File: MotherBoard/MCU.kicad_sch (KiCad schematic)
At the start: 0 parts

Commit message: Added IO Connector and uC
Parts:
- added U1: STM32F205RBTx, Package_QFP:LQFP-64_10x10mm_P0.5mm, symbol MCU_ST_STM32F2:STM32F205RBTx
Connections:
- new net: U1.18 (VSS), U1.63 (VSS)
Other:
- company: (none) -> FSAE LSU
- title: (none) -> STM32 Layout
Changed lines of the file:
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@@
 	(generator_version "8.0")
 	(paper "A4")
+	(title_block
+		(title "STM32 Layout")
+		(date "2024-10-15")
+		(rev "A")
+		(company "FSAE LSU")
+	)
+	(symbol
+		(lib_id "MCU_ST_STM32F2:STM32F205RBTx")
+		(at 143.51 92.71 0)
+		(unit 1)
+		(exclude_from_sim no)
+		(in_bom yes)
+		(on_board yes)
+		(dnp no)
+		(fields_autoplaced yes)
+		(property "Reference" "U1"
+			(at 148.2441 138.43 0)
+			(effects
+				(font
+					(size 1.27 1.27)
+				)
+				(justify left)
+			)
+		)
+		(property "Value" "STM32F205RBTx"
+			(at 148.2441 140.97 0)
+			(effects
+				(font
+					(size 1.27 1.27)
+				)
+				(justify left)
+			)
+		)
+		(property "Footprint" "Package_QFP:LQFP-64_10x10mm_P0.5mm"
+			(at 128.27 135.89 0)
+			(effects
+				(font
+					(size 1.27 1.27)
+				)
+				(justify right)
+				(hide yes)
+			)
+		)
+		(property "Datasheet" "https://www.st.com/resource/en/datasheet/stm32f205rb.pdf"
+			(at 143.51 92.71 0)
+			(effects
+				(font
+					(size 1.27 1.27)
+				)
+				(hide yes)
+			)
+		)
+		(property "Description" "STMicroelectronics Arm Cortex-M3 MCU, 128KB flash, 64KB RAM, 120 MHz, 1.8-3.6V, 51 GPIO, LQFP64"
+			(at 143.51 92.71 0)
+			(effects
+				(font
+					(size 1.27 1.27)
+				)
+				(hide yes)
+			)
+		)
+		(pin "46"
+		)
+		(pin "54"
+		)
+		(pin "58"
+		)
+		(pin "23"
+		)
+		(pin "16"
+		)
+		(pin "37"
+		)
+		(pin "44"
+		)
+		(pin "21"
+		)
+		(pin "38"
+		)
+		(pin "10"
+		)
+		(pin "45"
+		)
+		(pin "51"
+		)
+		(pin "52"
+		)
+		(pin "14"
+		)
+		(pin "36"
+		)
+		(pin "59"
+		)
+		(pin "18"
+		)
+		(pin "61"
+		)
+		(pin "62"
+		)
+		(pin "63"
+		)
+		(pin "15"
+		)
+		(pin "42"
+		)
+		(pin "43"
+		)
+		(pin "35"
+		)
+		(pin "29"
+		)
+		(pin "41"
+		)
+		(pin "53"
+		)
+		(pin "27"
+		)
+		(pin "33"
+		)
+		(pin "6"
+		)
+		(pin "2"
+		)
+		(pin "64"
+		)
+		(pin "26"
+		)
+		(pin "56"
+		)
+		(pin "47"
+		)
+		(pin "7"
+		)
+		(pin "4"
+		)
+		(pin "48"
+		)
+		(pin "34"
+		)
+		(pin "32"
+		)
+		(pin "40"
+		)
+		(pin "5"
+		)
+		(pin "60"
+		)
+		(pin "13"
+		)
+		(pin "22"
+		)
+		(pin "1"
+		)
+		(pin "20"
+		)
+		(pin "24"
+		)
+		(pin "39"
+		)
+		(pin "49"
+		)
+		(pin "31"
+		)
+		(pin "19"
+		)
+		(pin "55"
+		)
+		(pin "57"
+		)
+		(pin "8"
+		)
+		(pin "17"
+		)
+		(pin "28"
+		)
+		(pin "11"
+		)
+		(pin "25"
+		)
+		(pin "30"
+		)
+		(pin "3"
+		)
+		(pin "50"
+		)
+		(pin "12"
+		)
+		(pin "9"
+		)
+		(instances
+			(project ""
+				(path "/335e81e9-b957-4266-8116-dde74329bfca/592735c9-cbc0-4c76-b37a-83bb0c07029e"
+					(reference "U1")
+					(unit 1)
+				)
+			)
+		)
+	)
 )

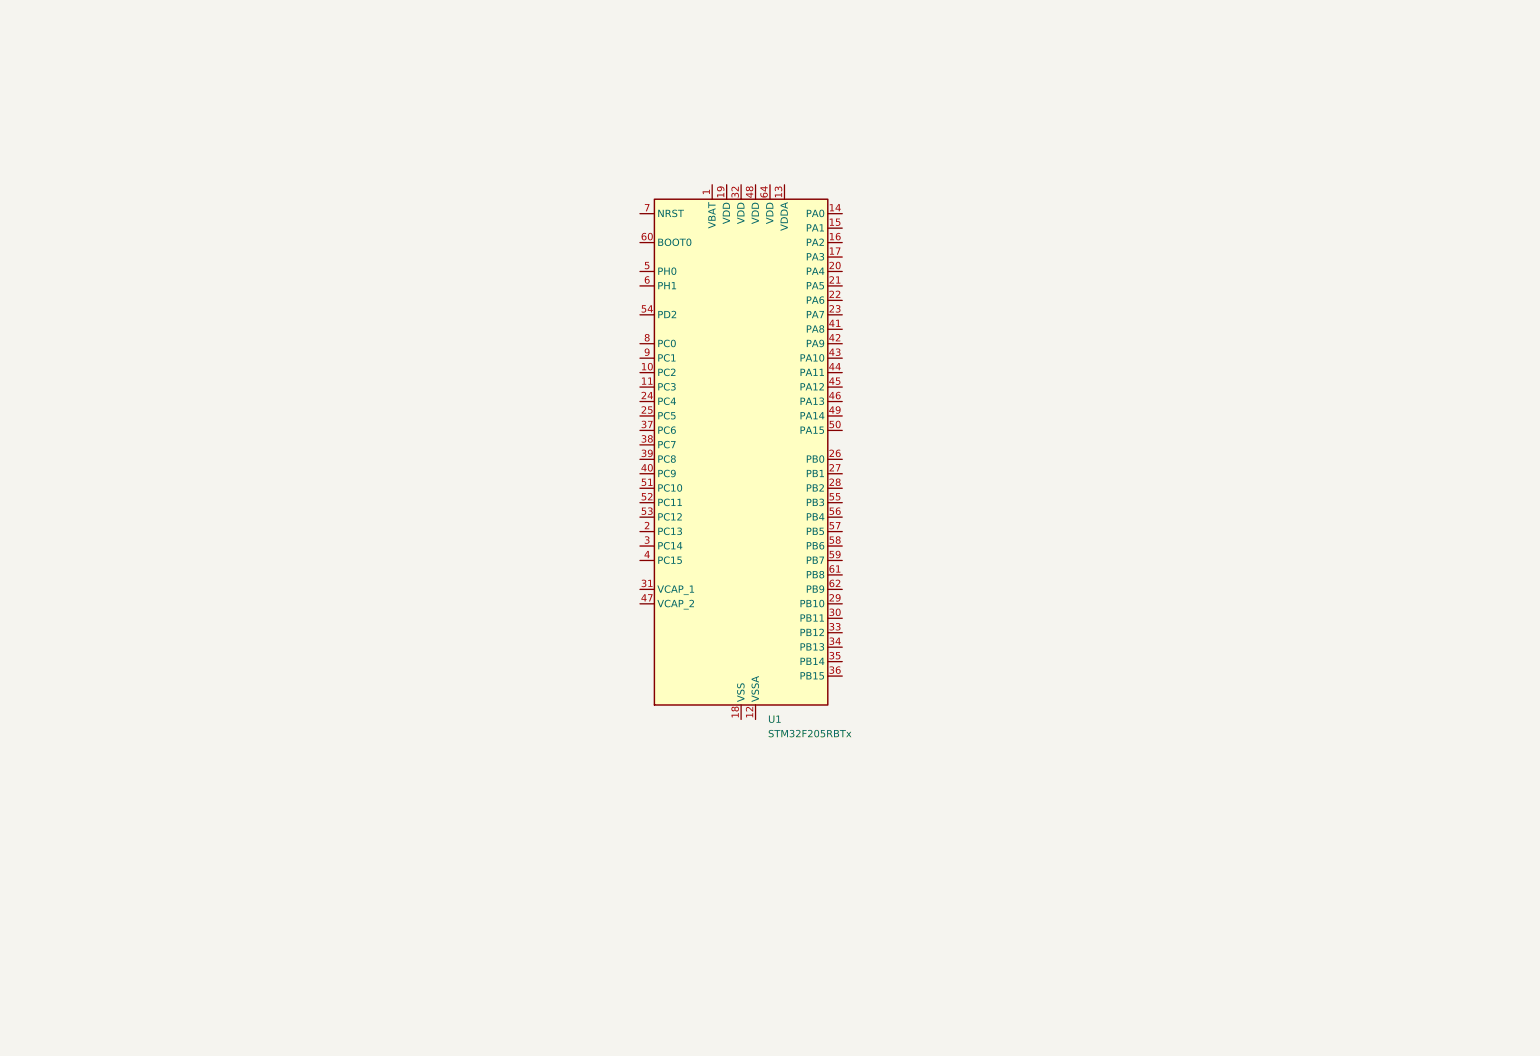
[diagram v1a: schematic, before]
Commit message: Complete bootstrap schematic for MCU
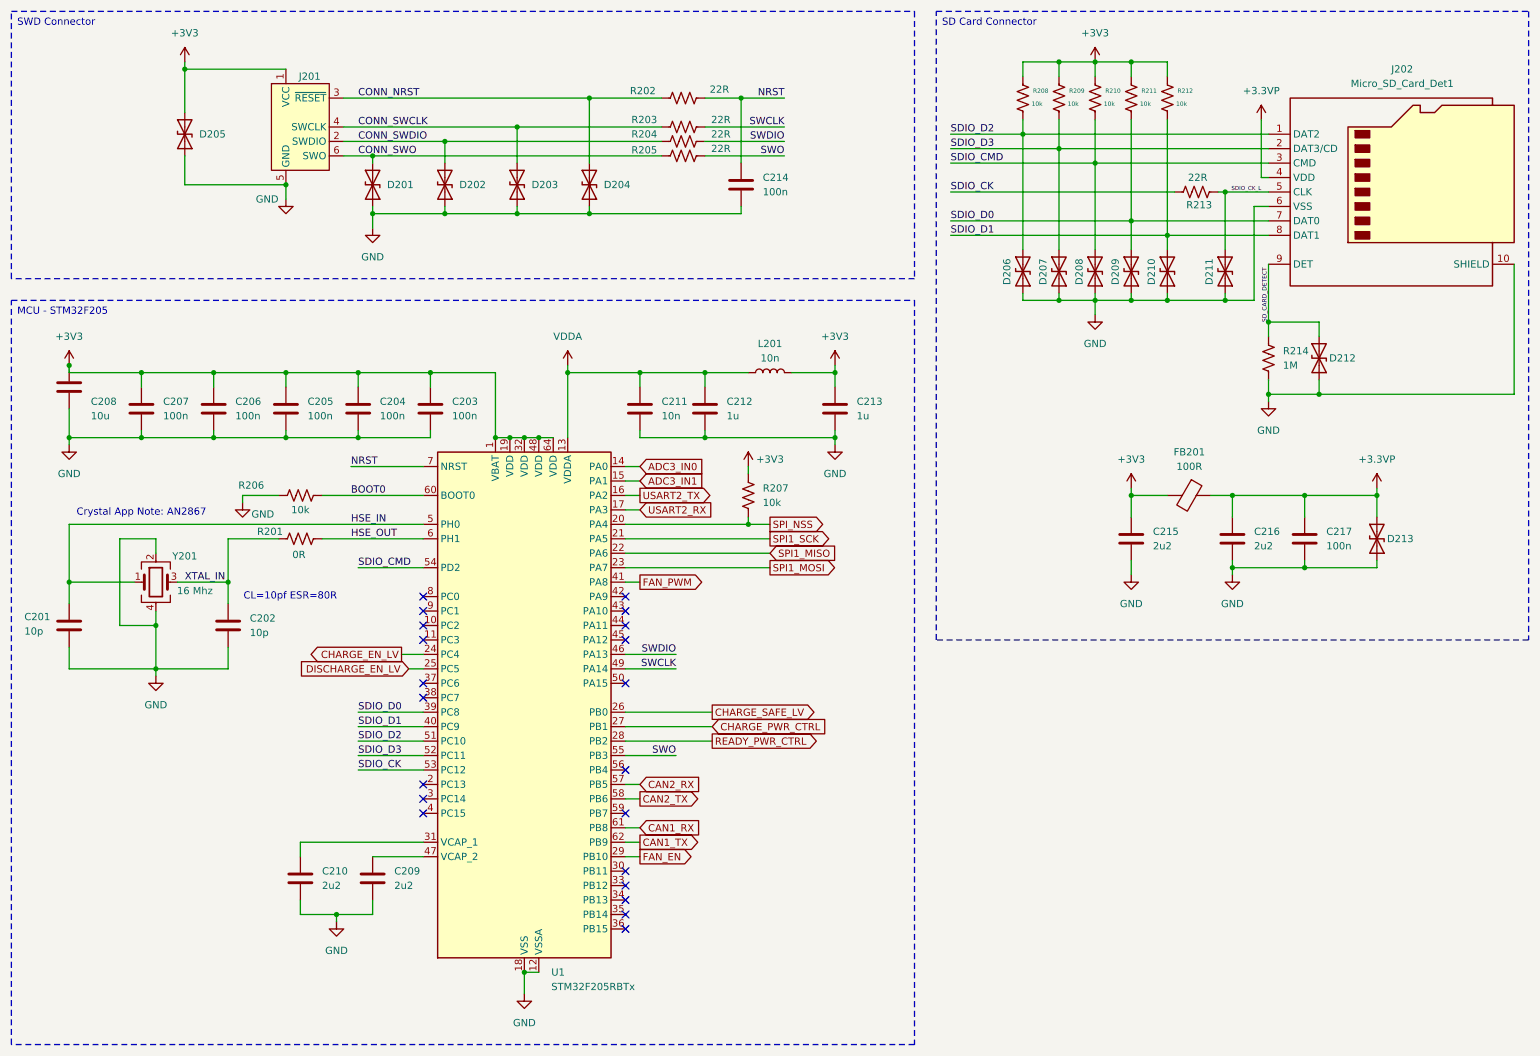
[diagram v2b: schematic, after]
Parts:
- added C201, C202: 10p, symbol Device:C
- added C203, C204, C205, C206, C207, C214, C217: 100n, symbol Device:C
- added C208: 10u, symbol Device:C
- added C209, C210, C215, C216: 2u2, symbol Device:C
- added C211: 10n, symbol Device:C
- added C212, C213: 1u, symbol Device:C
- added D201, D202, D203, D204, D205, D206, D207, D208, D209, D210, D211, D212, D213: 1N630xCA, Diode_THT:D_DO-201AE_P15.24mm_Horizontal, symbol Diode:1N630xCA
- added FB201: 100R, symbol Device:FerriteBead
- added J201: Conn_ARM_SWD_TagConnect_TC2030, Connector:Tag-Connect_TC2030-IDC-FP_2x03_P1.27mm_Vertical, symbol Connector:Conn_ARM_SWD_TagConnect_TC2030
- added J202: Micro_SD_Card_Det1, symbol Connector:Micro_SD_Card_Det1
- added L201: 10n, symbol Device:L
- added R201: 0R, symbol Device:R_US
- added R202, R203, R204, R205, R213: 22R, symbol Device:R_US
- added R206, R207, R208, R209, R210, R211, R212: 10k, symbol Device:R_US
- added R214: 1M, symbol Device:R_US
- added Y201: 16 Mhz, Crystal:Crystal_SMD_3225-4Pin_3.2x2.5mm, symbol Device:Crystal_GND24
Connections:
- net +3V3: now reaches U1.1 (VBAT)
- net +3V3: now also U1.19 (VDD), U1.32 (VDD), U1.48 (VDD), U1.64 (VDD), C203.1, C204.1, C205.1, C206.1, C207.1, C208.1, C213.1, C215.1, D205.2 (A2), FB201.2, J201.1 (VCC), L201.2, R207.1, R208.1, R209.1, R210.1, R211.1, R212.1
- net GND: now reaches U1.12 (VSSA)
- net GND: now also U1.18 (VSS), U1.63 (VSS), C201.2, C202.2, C203.2, C204.2, C205.2, C206.2, C207.2, C208.2, C209.2, C210.2, C211.2, C212.2, C213.2, C214.2, C215.2, C216.2, C217.2, D201.1 (A1), D202.1 (A1), D203.1 (A1), D204.1 (A1), D205.1 (A1), D206.1 (A1), D207.1 (A1), D208.1 (A1), D209.1 (A1), D210.1 (A1), D211.1 (A1), D212.1 (A1), D213.1 (A1), J201.5 (GND), J202.10 (SHIELD), J202.6 (VSS), R206.2, R214.2, Y201.2, Y201.4
- net VDDA: now reaches U1.13 (VDDA)
- net VDDA: now also C211.1, C212.1, L201.1
- net ADC3_IN0: now reaches U1.14 (PA0)
- net ADC3_IN1: now reaches U1.15 (PA1)
- net USART2_TX: now reaches U1.16 (PA2)
- net USART2_RX: now reaches U1.17 (PA3)
- net SPI_NSS: now reaches U1.20 (PA4)
- net SPI_NSS: now also R207.2
- net SPI1_SCK: now reaches U1.21 (PA5)
- net SPI1_MISO: now reaches U1.22 (PA6)
- net SPI1_MOSI: now reaches U1.23 (PA7)
- net CHARGE_EN_LV: now reaches U1.24 (PC4)
- net DISCHARGE_EN_LV: now reaches U1.25 (PC5)
- net CHARGE_SAFE_LV: now reaches U1.26 (PB0)
- net CHARGE_PWR_CTRL: now reaches U1.27 (PB1)
- net READY_PWR_CTRL: now reaches U1.28 (PB2)
- net FAN_EN: now reaches U1.29 (PB10)
- net at U1.31 (VCAP_1): now also C210.1
- net SDIO_D0: now reaches U1.39 (PC8)
- net SDIO_D0: now also D209.2 (A2), J202.7 (DAT0), R211.2
- net SDIO_D1: now reaches U1.40 (PC9)
- net SDIO_D1: now also D210.2 (A2), J202.8 (DAT1), R212.2
- net FAN_PWM: now reaches U1.41 (PA8)
- net SWDIO: now reaches U1.46 (PA13)
- net SWDIO: now also R204.2
- net at U1.47 (VCAP_2): now also C209.1
- net SWCLK: now reaches U1.49 (PA14)
- net SWCLK: now also R203.2
- net HSE_IN: now reaches U1.5 (PH0)
- net HSE_IN: now also C201.1, Y201.1
- net SDIO_D2: now reaches U1.51 (PC10)
- net SDIO_D2: now also D206.2 (A2), J202.1 (DAT2), R208.2
- net SDIO_D3: now reaches U1.52 (PC11)
- net SDIO_D3: now also D207.2 (A2), J202.2 (DAT3/CD), R209.2
- net SDIO_CK: now reaches U1.53 (PC12)
- net SDIO_CK: now also R213.1
- net SDIO_CMD: now reaches U1.54 (PD2)
- net SDIO_CMD: now also D208.2 (A2), J202.3 (CMD), R210.2
- net SWO: now reaches U1.55 (PB3)
- net SWO: now also R205.2
- net CAN2_RX: now reaches U1.57 (PB5)
- net CAN2_TX: now reaches U1.58 (PB6)
- net HSE_OUT: now reaches U1.6 (PH1)
- net HSE_OUT: now also R201.2
- net BOOT0: now reaches U1.60 (BOOT0)
- net BOOT0: now also R206.1
- net CAN1_RX: now reaches U1.61 (PB8)
- net CAN1_TX: now reaches U1.62 (PB9)
- net NRST: now reaches U1.7 (NRST)
- net NRST: now also C214.1, R202.2
- new net +3.3VP: C216.1, C217.1, D213.2 (A2), FB201.1, J202.4 (VDD)
- new net CONN_NRST: D204.2 (A2), J201.3 (~{RESET}), R202.1
- new net CONN_SWCLK: D203.2 (A2), J201.4 (SWCLK), R203.1
- new net CONN_SWDIO: D202.2 (A2), J201.2 (SWDIO), R204.1
- new net CONN_SWO: D201.2 (A2), J201.6 (SWO), R205.1
- new net SDIO_CK_L: D211.2 (A2), J202.5 (CLK), R213.2
- new net SD_CARD_DETECT: D212.2 (A2), J202.9 (DET), R214.1
- new net XTAL_IN: C202.1, R201.1, Y201.3
- no-connect marks 0 -> 21
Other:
- note added: "CL=10pf ESR=80R"
- note added: "Crystal App Note: AN2867"
- moved on the sheet: U1

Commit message: PSU Complete
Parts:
- removed D207, D208, D209, D210, D211: 1N630xCA, Diode_THT:D_DO-201AE_P15.24mm_Horizontal, symbol Diode:1N630xCA
- added D207, D208, D209, D210, D211: D_TVS, Diode_SMD:D_SOD-323, symbol Device:D_TVS
- D201: renamed from D205; value 1N630xCA -> D_TVS; footprint Diode_THT:D_DO-201AE_P15.24mm_Horizontal -> Diode_SMD:D_SOD-323; symbol Diode:1N630xCA -> Device:D_TVS
- D202: renamed from D201; value 1N630xCA -> D_TVS; footprint Diode_THT:D_DO-201AE_P15.24mm_Horizontal -> Diode_SMD:D_SOD-323; symbol Diode:1N630xCA -> Device:D_TVS
- D203: renamed from D202; value 1N630xCA -> D_TVS; footprint Diode_THT:D_DO-201AE_P15.24mm_Horizontal -> Diode_SMD:D_SOD-323; symbol Diode:1N630xCA -> Device:D_TVS
- D204: renamed from D203; value 1N630xCA -> D_TVS; footprint Diode_THT:D_DO-201AE_P15.24mm_Horizontal -> Diode_SMD:D_SOD-323; symbol Diode:1N630xCA -> Device:D_TVS
- D205: renamed from D204; value 1N630xCA -> D_TVS; footprint Diode_THT:D_DO-201AE_P15.24mm_Horizontal -> Diode_SMD:D_SOD-323; symbol Diode:1N630xCA -> Device:D_TVS
- D206, D212, D213: value 1N630xCA -> D_TVS; footprint Diode_THT:D_DO-201AE_P15.24mm_Horizontal -> Diode_SMD:D_SOD-323; symbol Diode:1N630xCA -> Device:D_TVS
- R201: renamed from R206; footprint (none) -> Resistor_SMD:R_0402_1005Metric
- R202: renamed from R201; footprint (none) -> Resistor_SMD:R_0402_1005Metric
- R203: renamed from R202; footprint (none) -> Resistor_SMD:R_0402_1005Metric
- R204: renamed from R203; footprint (none) -> Resistor_SMD:R_0402_1005Metric
- R205: renamed from R204; footprint (none) -> Resistor_SMD:R_0402_1005Metric
- R206: renamed from R205; footprint (none) -> Resistor_SMD:R_0402_1005Metric
- R207, R208, R209, R210, R211, R212, R213, R214: footprint (none) -> Resistor_SMD:R_0402_1005Metric
- renumbered C208 to C201, C201 to C202, C207 to C203, C206 to C204, C202 to C205, C205 to C206, C210 to C207, C204 to C208, C203 to C210, C214 to C213, C213 to C214, U1 to U201
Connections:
- net GND: now also D207.1 (A1), D208.1 (A1), D209.1 (A1), D210.1 (A1), D211.1 (A1)
- net SDIO_CK_L: now also D211.2 (A2)
- net SDIO_CMD: now also D208.2 (A2)
- net SDIO_D0: now also D209.2 (A2)
- net SDIO_D1: now also D210.2 (A2)
- net SDIO_D3: now also D207.2 (A2)
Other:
- note added: "100mA Max"
- note added: "120mA Max ~40mA Typ"
- note added: ">2 Ohm ESR"

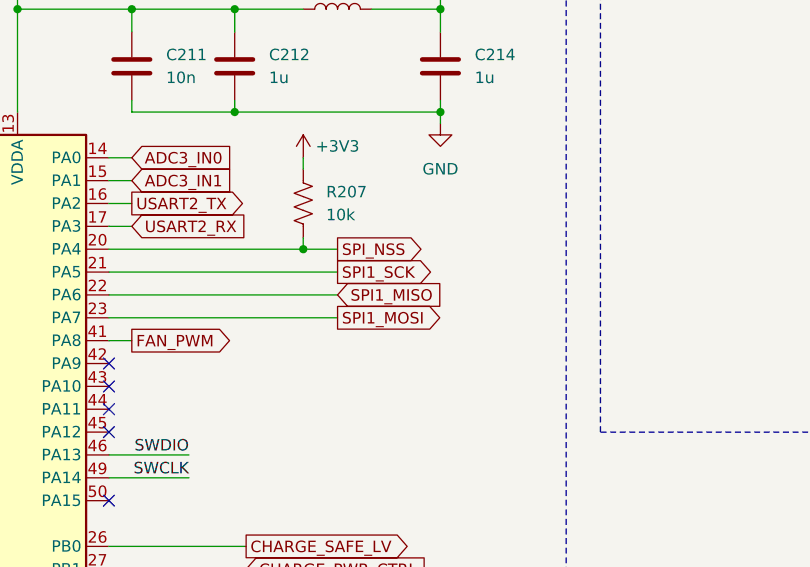
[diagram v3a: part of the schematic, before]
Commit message: Added BQ7900 rough draft and TCAN
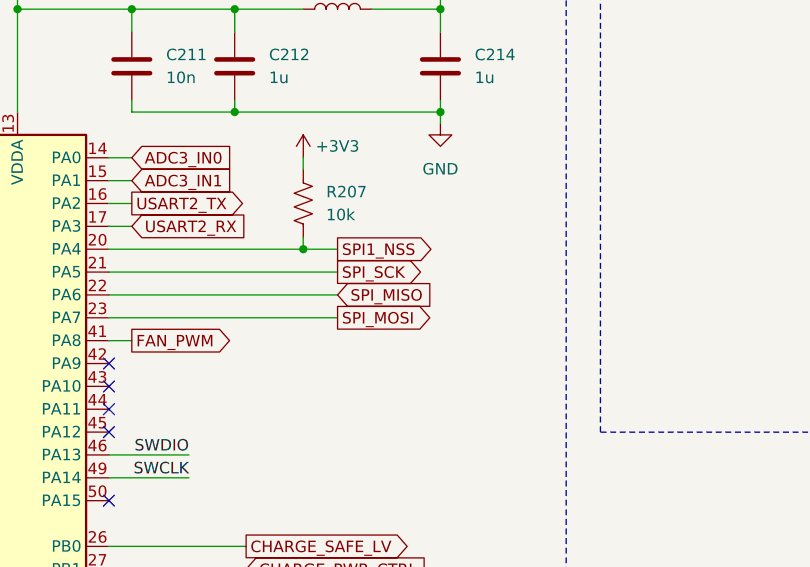
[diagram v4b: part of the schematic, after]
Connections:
- net SPI1_MISO renamed SPI_MISO
- net SPI1_MOSI renamed SPI_MOSI
- net SPI1_SCK renamed SPI_SCK
- net SPI_NSS renamed SPI1_NSS
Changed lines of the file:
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@@
 		)
 	)
-	(global_label "SPI1_MOSI"
+	(global_label "SPI_MOSI"
 		(shape output)
 		(at 148.59 111.76 0)
@@
 		)
 		(property "Intersheetrefs" "${INTERSHEET_REFS}"
-			(at 161.4328 111.76 0)
+			(at 160.2233 111.76 0)
 			(effects
 				(font
@@
 		)
 	)
-	(global_label "SPI_NSS"
+	(global_label "SPI1_NSS"
 		(shape output)
 		(at 148.59 104.14 0)
@@
 		)
 		(property "Intersheetrefs" "${INTERSHEET_REFS}"
-			(at 159.3766 104.14 0)
+			(at 160.5861 104.14 0)
 			(effects
 				(font
@@
 		)
 	)
-	(global_label "SPI1_MISO"
+	(global_label "SPI_MISO"
 		(shape input)
 		(at 148.59 109.22 0)
@@
 		)
 		(property "Intersheetrefs" "${INTERSHEET_REFS}"
-			(at 161.4328 109.22 0)
+			(at 160.2233 109.22 0)
 			(effects
 				(font
@@
 		)
 	)
-	(global_label "SPI1_SCK"
+	(global_label "SPI_SCK"
 		(shape output)
 		(at 148.59 106.68 0)
@@
 		)
 		(property "Intersheetrefs" "${INTERSHEET_REFS}"
-			(at 160.5861 106.68 0)
-			(effects
-				(font
+			(at 159.3766 106.68 0)
+			(effects
+				(font
